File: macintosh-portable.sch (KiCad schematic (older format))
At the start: 0 parts

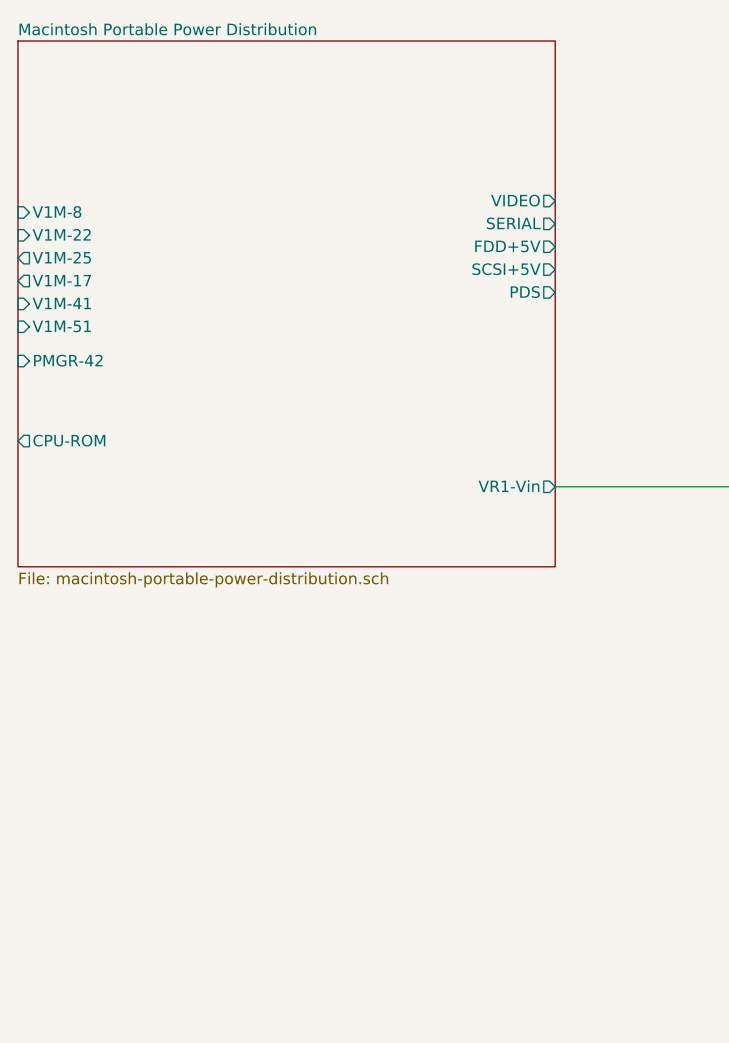
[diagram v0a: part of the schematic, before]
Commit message: Added V1M module.
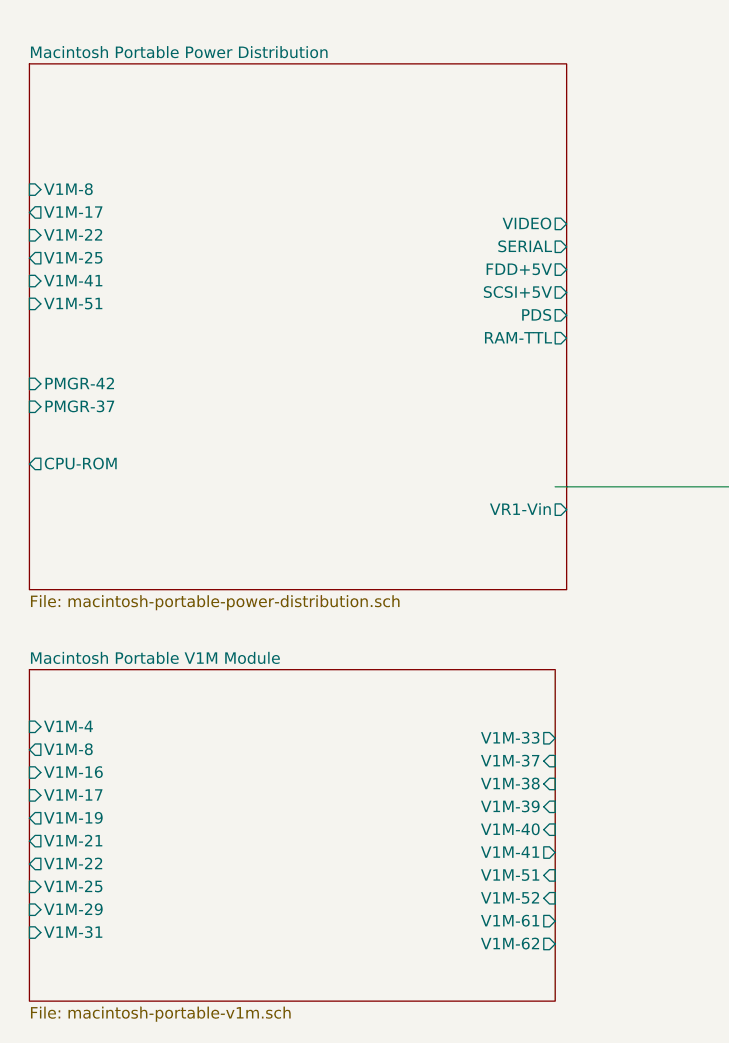
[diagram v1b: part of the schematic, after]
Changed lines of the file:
@@
 $Descr A4 11693 8268
 encoding utf-8
-Sheet 1 3
+Sheet 1 4
 Title ""
 Date ""
@@
 $EndDescr
 $Sheet
-S 1150 1400 2350 2300
+S 1200 1500 2350 2300
 U 5CE45908
 F0 "Macintosh Portable Power Distribution" 50
 F1 "macintosh-portable-power-distribution.sch" 50
-F2 "VR1-Vin" O R 3500 3350 50
-F3 "V1M-41" I L 1150 2550 50
-F4 "V1M-51" I L 1150 2650 50
-F5 "PMGR-42" I L 1150 2800 50
-F6 "SCSI+5V" O R 3500 2400 50
-F7 "V1M-8" I L 1150 2150 50
-F8 "FDD+5V" O R 3500 2300 50
-F9 "CPU-ROM" O L 1150 3150 50
-F10 "PDS" O R 3500 2500 50
-F11 "VIDEO" O R 3500 2100 50
-F12 "SERIAL" O R 3500 2200 50
-F13 "V1M-25" O L 1150 2350 50
-F14 "V1M-17" O L 1150 2450 50
-F15 "V1M-22" I L 1150 2250 50
+F2 "VR1-Vin" O R 3550 3450 50
+F3 "V1M-41" I L 1200 2450 50
+F4 "V1M-51" I L 1200 2550 50
+F5 "PMGR-42" I L 1200 2900 50
+F6 "SCSI+5V" O R 3550 2500 50
+F7 "V1M-8" I L 1200 2050 50
+F8 "FDD+5V" O R 3550 2400 50
+F9 "CPU-ROM" O L 1200 3250 50
+F10 "PDS" O R 3550 2600 50
+F11 "VIDEO" O R 3550 2200 50
+F12 "SERIAL" O R 3550 2300 50
+F13 "V1M-25" O L 1200 2350 50
+F14 "V1M-17" O L 1200 2150 50
+F15 "V1M-22" I L 1200 2250 50
+F16 "RAM-TTL" O R 3550 2700 50
+F17 "PMGR-37" I L 1200 3000 50
 $EndSheet
 $Sheet
@@
 Wire Wire Line
 	3500 3350 4550 3350
+$Sheet
+S 1200 4150 2300 1450
+U 5CE523FB
+F0 "Macintosh Portable V1M Module" 50
+F1 "macintosh-portable-v1m.sch" 50
+F2 "V1M-22" O L 1200 5000 50
+F3 "V1M-16" I L 1200 4600 50
+F4 "V1M-17" I L 1200 4700 50
+F5 "V1M-40" I R 3500 4850 50
+F6 "V1M-29" I L 1200 5200 50
+F7 "V1M-31" I L 1200 5300 50
+F8 "V1M-25" I L 1200 5100 50
+F9 "V1M-37" I R 3500 4550 50
+F10 "V1M-51" I R 3500 5050 50
+F11 "V1M-52" I R 3500 5150 50
+F12 "V1M-62" O R 3500 5350 50
+F13 "V1M-8" O L 1200 4500 50
+F14 "V1M-4" I L 1200 4400 50
+F15 "V1M-39" I R 3500 4750 50
+F16 "V1M-38" I R 3500 4650 50
+F17 "V1M-41" O R 3500 4950 50
+F18 "V1M-19" O L 1200 4800 50
+F19 "V1M-21" O L 1200 4900 50
+F20 "V1M-33" O R 3500 4450 50
+F21 "V1M-61" O R 3500 5250 50
+$EndSheet
 $EndSCHEMATC

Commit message: Finished V1M, more references on other sheets.
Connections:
- wire segments 1 -> 17
- no-connect marks 0 -> 2
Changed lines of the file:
@@
 encoding utf-8
 Sheet 1 4
-Title ""
-Date ""
-Rev "0.1"
-Comp ""
-Comment1 ""
+Title "Macintosh Portable Power"
+Date "2019-05-27"
+Rev "0.12"
+Comp "https://oldcrap.org"
+Comment1 "Author: Pawel Pieczul"
 Comment2 ""
 Comment3 ""
@@
 $EndDescr
 $Sheet
-S 1200 1500 2350 2300
+S 4100 2100 2350 2400
 U 5CE45908
 F0 "Macintosh Portable Power Distribution" 50
 F1 "macintosh-portable-power-distribution.sch" 50
-F2 "VR1-Vin" O R 3550 3450 50
-F3 "V1M-41" I L 1200 2450 50
-F4 "V1M-51" I L 1200 2550 50
-F5 "PMGR-42" I L 1200 2900 50
-F6 "SCSI+5V" O R 3550 2500 50
-F7 "V1M-8" I L 1200 2050 50
-F8 "FDD+5V" O R 3550 2400 50
-F9 "CPU-ROM" O L 1200 3250 50
-F10 "PDS" O R 3550 2600 50
-F11 "VIDEO" O R 3550 2200 50
-F12 "SERIAL" O R 3550 2300 50
-F13 "V1M-25" O L 1200 2350 50
-F14 "V1M-17" O L 1200 2150 50
-F15 "V1M-22" I L 1200 2250 50
-F16 "RAM-TTL" O R 3550 2700 50
-F17 "PMGR-37" I L 1200 3000 50
+F2 "VR1-Vin" O R 6450 4050 50
+F3 "V1M-41" I L 4100 3450 50
+F4 "V1M-51" I L 4100 3550 50
+F5 "PMGR-42" I L 4100 4150 50
+F6 "SCSI+5V" O R 6450 2650 50
+F7 "V1M-8" I L 4100 2450 50
+F8 "FDD+5V" O R 6450 2550 50
+F9 "CPU-ROM" O R 6450 2950 50
+F10 "PDS" O R 6450 2750 50
+F11 "VIDEO" O R 6450 2450 50
+F12 "V1M-25" O L 4100 3050 50
+F13 "V1M-17" O L 4100 2750 50
+F14 "V1M-22" I L 4100 2950 50
+F15 "RAM-TTL" O R 6450 2850 50
+F16 "PMGR-37" I L 4100 4250 50
+F17 "SERIAL-VCC" O R 6450 3050 50
+F18 "V1M-52" I L 4100 3650 50
+F19 "V1M-39" O L 4100 3350 50
+F20 "V1M-16" O L 4100 2650 50
+F21 "V1M-62" I L 4100 3750 50
+F22 "J21-31" O L 4100 3150 50
+F23 "PMGR-52" O L 4100 4350 50
+F24 "V1M-33" I L 4100 3250 50
+F25 "J9-10" O R 6450 3550 50
+F26 "V1M-18" O L 4100 2850 50
+F27 "V1M-11" O L 4100 2550 50
+F28 "SERIAL-VEE" O R 6450 3150 50
 $EndSheet
 $Sheet
-S 4550 2600 1950 900
+S 6800 3750 1850 450
 U 5CFAA7F4
 F0 "Macintosh Portable 12V Generator Circuit" 50
 F1 "macintosh-portable-12v-generator.sch" 50
-F2 "VR1-Vin" I L 4550 3350 50
-F3 "SCSI+12V" O R 6500 2950 50
-F4 "FDD+12V" O R 6500 3200 50
+F2 "VR1-Vin" I L 6800 4050 50
+F3 "SCSI+12V" O R 8650 3900 50
+F4 "FDD+12V" O R 8650 4050 50
 $EndSheet
 Wire Wire Line
-	3500 3350 4550 3350
+	6450 4050 6800 4050
 $Sheet
-S 1200 4150 2300 1450
+S 1350 900  2350 3600
 U 5CE523FB
 F0 "Macintosh Portable V1M Module" 50
 F1 "macintosh-portable-v1m.sch" 50
-F2 "V1M-22" O L 1200 5000 50
-F3 "V1M-16" I L 1200 4600 50
-F4 "V1M-17" I L 1200 4700 50
-F5 "V1M-40" I R 3500 4850 50
-F6 "V1M-29" I L 1200 5200 50
-F7 "V1M-31" I L 1200 5300 50
-F8 "V1M-25" I L 1200 5100 50
-F9 "V1M-37" I R 3500 4550 50
-F10 "V1M-51" I R 3500 5050 50
-F11 "V1M-52" I R 3500 5150 50
-F12 "V1M-62" O R 3500 5350 50
-F13 "V1M-8" O L 1200 4500 50
-F14 "V1M-4" I L 1200 4400 50
-F15 "V1M-39" I R 3500 4750 50
-F16 "V1M-38" I R 3500 4650 50
-F17 "V1M-41" O R 3500 4950 50
-F18 "V1M-19" O L 1200 4800 50
-F19 "V1M-21" O L 1200 4900 50
-F20 "V1M-33" O R 3500 4450 50
-F21 "V1M-61" O R 3500 5250 50
+F2 "V1M-22" O R 3700 2950 50
+F3 "V1M-16" I R 3700 2650 50
+F4 "V1M-17" I R 3700 2750 50
+F5 "V1M-40" I R 3700 1600 50
+F6 "V1M-29" I L 1350 2200 50
+F7 "V1M-31" I R 3700 3150 50
+F8 "V1M-25" I R 3700 3050 50
+F9 "V1M-37" I R 3700 1300 50
+F10 "V1M-51" O R 3700 3550 50
+F11 "V1M-52" O R 3700 3650 50
+F12 "V1M-62" O R 3700 3750 50
+F13 "V1M-8" O R 3700 2450 50
+F14 "V1M-4" I L 1350 1000 50
+F15 "V1M-39" I R 3700 3350 50
+F16 "V1M-38" I R 3700 1400 50
+F17 "V1M-41" O R 3700 3450 50
+F18 "V1M-19" O L 1350 1700 50
+F19 "V1M-21" O L 1350 1900 50
+F20 "V1M-33" O R 3700 3250 50
+F21 "V1M-61" O R 3700 2100 50
+F22 "V1M-5" O L 1350 1100 50
+F23 "V1M-20" O L 1350 1800 50
+F24 "V1M-36" O R 3700 1200 50
+F25 "V1M-59" O R 3700 2000 50
+F26 "V1M-11" I R 3700 2550 50
+F27 "V1M-18" I R 3700 2850 50
 $EndSheet
+NoConn ~ 1100 1900
+NoConn ~ 3800 2100
+Wire Wire Line
+	3800 2100 3700 2100
+Wire Wire Line
+	1100 1900 1350 1900
+Wire Wire Line
+	3700 2450 4100 2450
+Wire Wire Line
+	3700 2550 4100 2550
+Wire Wire Line
+	4100 2650 3700 2650
+Wire Wire Line
+	4100 2750 3700 2750
+Wire Wire Line
+	4100 2850 3700 2850
+Wire Wire Line
+	3700 2950 4100 2950
+Wire Wire Line
+	4100 3050 3700 3050
+Wire Wire Line
+	4100 3150 3700 3150
+Wire Wire Line
+	3700 3250 4100 3250
+Wire Wire Line
+	4100 3350 3700 3350
+Wire Wire Line
+	3700 3450 4100 3450
+Wire Wire Line
+	3700 3550 4100 3550
+Wire Wire Line
+	3700 3650 4100 3650
+Wire Wire Line
+	3700 3750 4100 3750
 $EndSCHEMATC

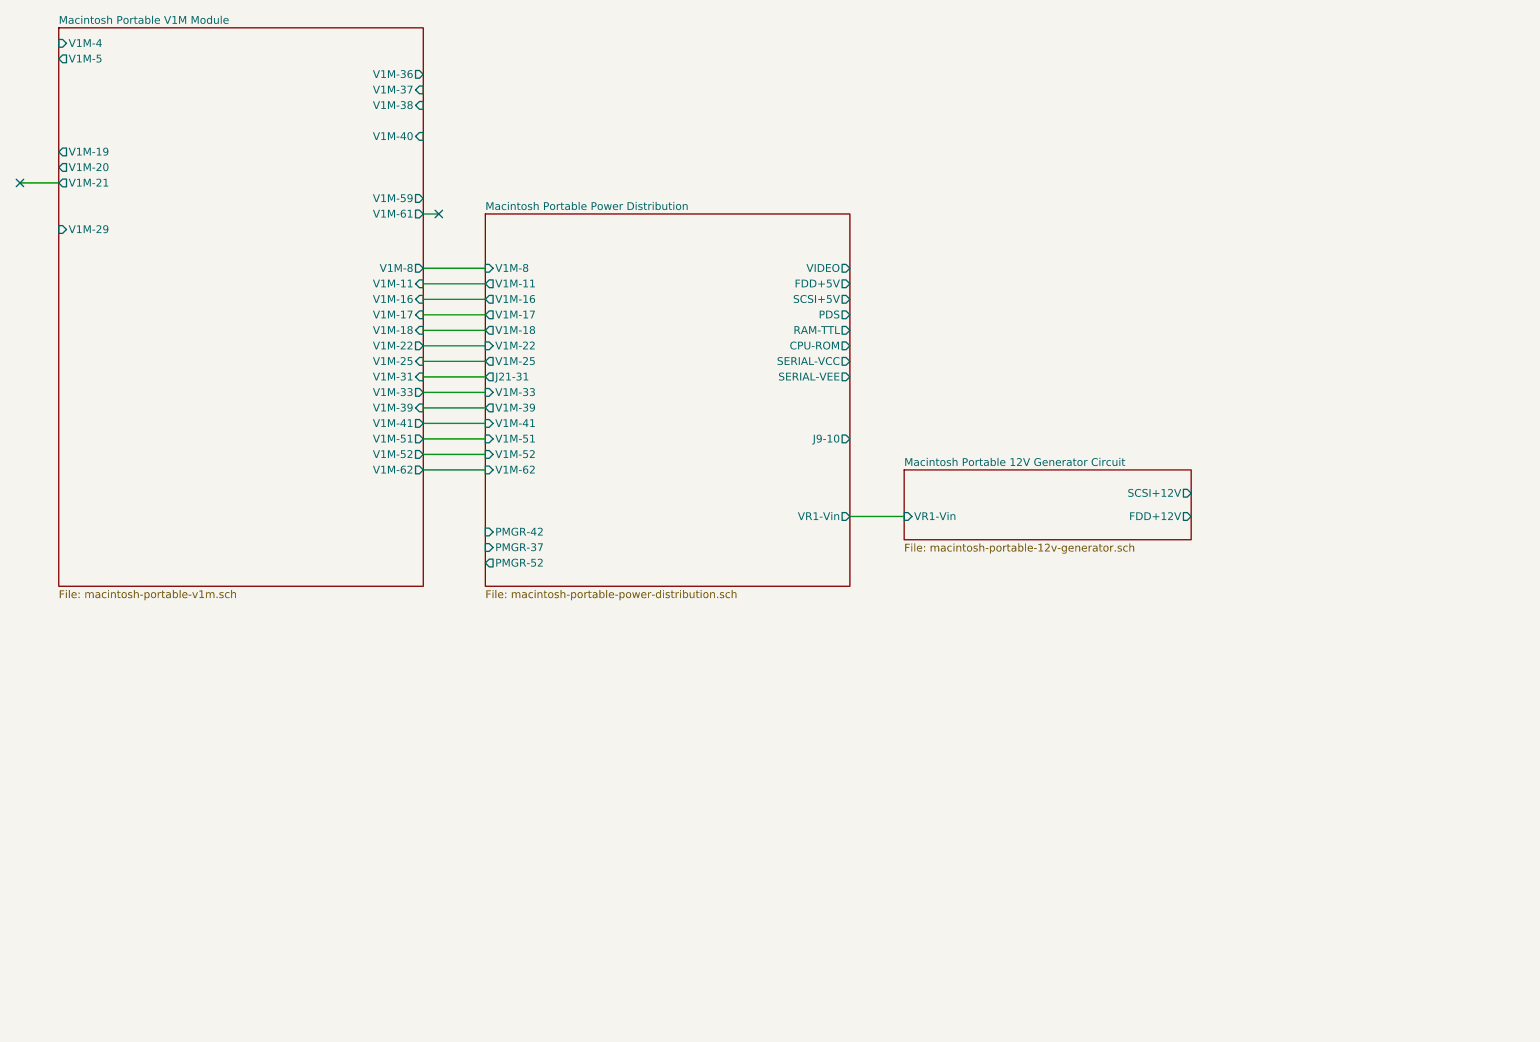
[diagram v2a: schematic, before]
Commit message: Symbol library cleanup
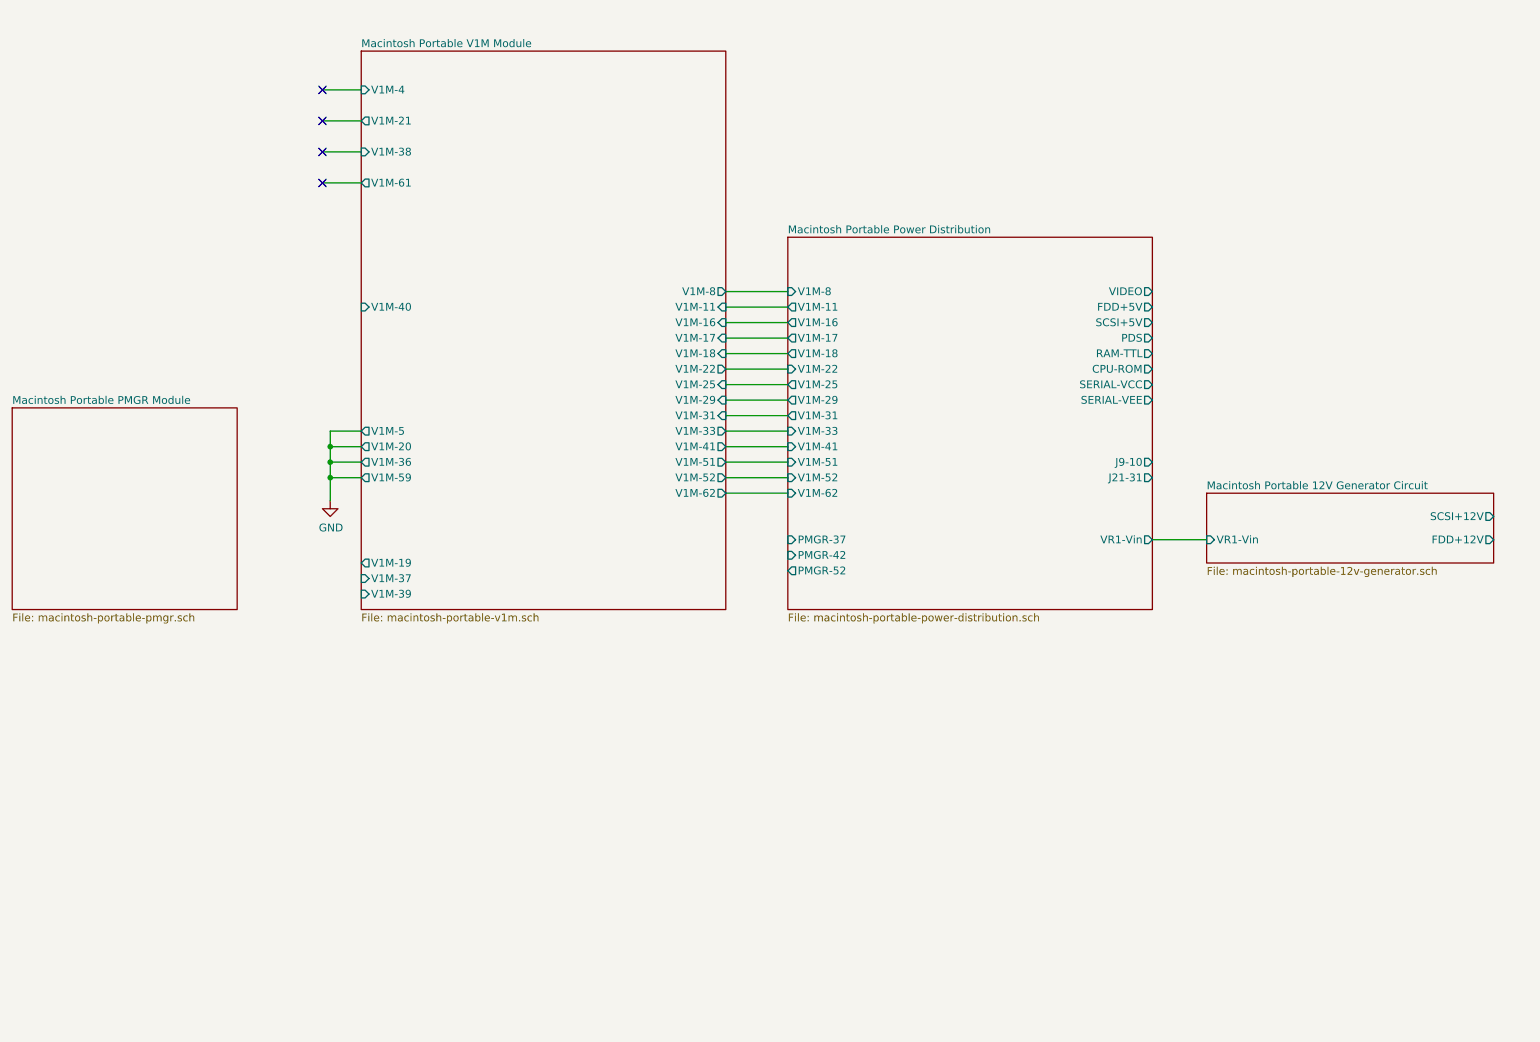
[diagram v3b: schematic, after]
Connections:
- no-connect marks 2 -> 4
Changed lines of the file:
@@
 $Descr A4 11693 8268
 encoding utf-8
-Sheet 1 4
+Sheet 1 5
 Title "Macintosh Portable Power"
 Date "2019-05-27"
@@
 $EndDescr
 $Sheet
-S 4100 2100 2350 2400
+S 6050 2250 2350 2400
 U 5CE45908
 F0 "Macintosh Portable Power Distribution" 50
 F1 "macintosh-portable-power-distribution.sch" 50
-F2 "VR1-Vin" O R 6450 4050 50
-F3 "V1M-41" I L 4100 3450 50
-F4 "V1M-51" I L 4100 3550 50
-F5 "PMGR-42" I L 4100 4150 50
-F6 "SCSI+5V" O R 6450 2650 50
-F7 "V1M-8" I L 4100 2450 50
-F8 "FDD+5V" O R 6450 2550 50
-F9 "CPU-ROM" O R 6450 2950 50
-F10 "PDS" O R 6450 2750 50
-F11 "VIDEO" O R 6450 2450 50
-F12 "V1M-25" O L 4100 3050 50
-F13 "V1M-17" O L 4100 2750 50
-F14 "V1M-22" I L 4100 2950 50
-F15 "RAM-TTL" O R 6450 2850 50
-F16 "PMGR-37" I L 4100 4250 50
-F17 "SERIAL-VCC" O R 6450 3050 50
-F18 "V1M-52" I L 4100 3650 50
-F19 "V1M-39" O L 4100 3350 50
-F20 "V1M-16" O L 4100 2650 50
-F21 "V1M-62" I L 4100 3750 50
-F22 "J21-31" O L 4100 3150 50
-F23 "PMGR-52" O L 4100 4350 50
-F24 "V1M-33" I L 4100 3250 50
-F25 "J9-10" O R 6450 3550 50
-F26 "V1M-18" O L 4100 2850 50
-F27 "V1M-11" O L 4100 2550 50
-F28 "SERIAL-VEE" O R 6450 3150 50
+F2 "VR1-Vin" O R 8400 4200 50
+F3 "V1M-41" I L 6050 3600 50
+F4 "V1M-51" I L 6050 3700 50
+F5 "PMGR-42" I L 6050 4300 50
+F6 "SCSI+5V" O R 8400 2800 50
+F7 "V1M-8" I L 6050 2600 50
+F8 "FDD+5V" O R 8400 2700 50
+F9 "CPU-ROM" O R 8400 3100 50
+F10 "PDS" O R 8400 2900 50
+F11 "VIDEO" O R 8400 2600 50
+F12 "V1M-25" O L 6050 3200 50
+F13 "V1M-17" O L 6050 2900 50
+F14 "V1M-22" I L 6050 3100 50
+F15 "RAM-TTL" O R 8400 3000 50
+F16 "PMGR-37" I L 6050 4200 50
+F17 "SERIAL-VCC" O R 8400 3200 50
+F18 "V1M-52" I L 6050 3800 50
+F19 "V1M-16" O L 6050 2800 50
+F20 "V1M-62" I L 6050 3900 50
+F21 "J21-31" O R 8400 3800 50
+F22 "PMGR-52" O L 6050 4400 50
+F23 "V1M-33" I L 6050 3500 50
+F24 "J9-10" O R 8400 3700 50
+F25 "V1M-18" O L 6050 3000 50
+F26 "V1M-11" O L 6050 2700 50
+F27 "SERIAL-VEE" O R 8400 3300 50
+F28 "V1M-31" O L 6050 3400 50
+F29 "V1M-29" O L 6050 3300 50
 $EndSheet
 $Sheet
-S 6800 3750 1850 450
+S 8750 3900 1850 450
 U 5CFAA7F4
 F0 "Macintosh Portable 12V Generator Circuit" 50
 F1 "macintosh-portable-12v-generator.sch" 50
-F2 "VR1-Vin" I L 6800 4050 50
-F3 "SCSI+12V" O R 8650 3900 50
-F4 "FDD+12V" O R 8650 4050 50
+F2 "VR1-Vin" I L 8750 4200 50
+F3 "SCSI+12V" O R 10600 4050 50
+F4 "FDD+12V" O R 10600 4200 50
 $EndSheet
 Wire Wire Line
-	6450 4050 6800 4050
+	8400 4200 8750 4200
 $Sheet
-S 1350 900  2350 3600
+S 3300 1050 2350 3600
 U 5CE523FB
 F0 "Macintosh Portable V1M Module" 50
 F1 "macintosh-portable-v1m.sch" 50
-F2 "V1M-22" O R 3700 2950 50
-F3 "V1M-16" I R 3700 2650 50
-F4 "V1M-17" I R 3700 2750 50
-F5 "V1M-40" I R 3700 1600 50
-F6 "V1M-29" I L 1350 2200 50
-F7 "V1M-31" I R 3700 3150 50
-F8 "V1M-25" I R 3700 3050 50
-F9 "V1M-37" I R 3700 1300 50
-F10 "V1M-51" O R 3700 3550 50
-F11 "V1M-52" O R 3700 3650 50
-F12 "V1M-62" O R 3700 3750 50
-F13 "V1M-8" O R 3700 2450 50
-F14 "V1M-4" I L 1350 1000 50
-F15 "V1M-39" I R 3700 3350 50
-F16 "V1M-38" I R 3700 1400 50
-F17 "V1M-41" O R 3700 3450 50
-F18 "V1M-19" O L 1350 1700 50
-F19 "V1M-21" O L 1350 1900 50
-F20 "V1M-33" O R 3700 3250 50
-F21 "V1M-61" O R 3700 2100 50
-F22 "V1M-5" O L 1350 1100 50
-F23 "V1M-20" O L 1350 1800 50
-F24 "V1M-36" O R 3700 1200 50
-F25 "V1M-59" O R 3700 2000 50
-F26 "V1M-11" I R 3700 2550 50
-F27 "V1M-18" I R 3700 2850 50
+F2 "V1M-22" O R 5650 3100 50
+F3 "V1M-16" I R 5650 2800 50
+F4 "V1M-17" I R 5650 2900 50
+F5 "V1M-40" I L 3300 2700 50
+F6 "V1M-29" I R 5650 3300 50
+F7 "V1M-31" I R 5650 3400 50
+F8 "V1M-25" I R 5650 3200 50
+F9 "V1M-37" I L 3300 4450 50
+F10 "V1M-51" O R 5650 3700 50
+F11 "V1M-52" O R 5650 3800 50
+F12 "V1M-62" O R 5650 3900 50
+F13 "V1M-8" O R 5650 2600 50
+F14 "V1M-4" I L 3300 1300 50
+F15 "V1M-39" I L 3300 4550 50
+F16 "V1M-38" I L 3300 1700 50
+F17 "V1M-41" O R 5650 3600 50
+F18 "V1M-19" O L 3300 4350 50
+F19 "V1M-21" O L 3300 1500 50
+F20 "V1M-33" O R 5650 3500 50
+F21 "V1M-61" O L 3300 1900 50
+F22 "V1M-5" O L 3300 3500 50
+F23 "V1M-20" O L 3300 3600 50
+F24 "V1M-36" O L 3300 3700 50
+F25 "V1M-59" O L 3300 3800 50
+F26 "V1M-11" I R 5650 2700 50
+F27 "V1M-18" I R 5650 3000 50
 $EndSheet
-NoConn ~ 1100 1900
-NoConn ~ 3800 2100
+NoConn ~ 3050 1500
 Wire Wire Line
-	3800 2100 3700 2100
+	3050 1500 3300 1500
 Wire Wire Line
-	1100 1900 1350 1900
+	5650 2600 6050 2600
 Wire Wire Line
-	3700 2450 4100 2450
+	5650 2700 6050 2700
 Wire Wire Line
-	3700 2550 4100 2550
+	6050 2800 5650 2800
 Wire Wire Line
-	4100 2650 3700 2650
+	6050 2900 5650 2900
 Wire Wire Line
-	4100 2750 3700 2750
+	6050 3000 5650 3000
 Wire Wire Line
-	4100 2850 3700 2850
+	5650 3100 6050 3100
 Wire Wire Line
-	3700 2950 4100 2950
+	6050 3200 5650 3200
 Wire Wire Line
-	4100 3050 3700 3050
+	6050 3400 5650 3400
 Wire Wire Line
-	4100 3150 3700 3150
+	5650 3500 6050 3500
 Wire Wire Line
-	3700 3250 4100 3250
+	5650 3600 6050 3600
 Wire Wire Line
-	4100 3350 3700 3350
+	5650 3700 6050 3700
 Wire Wire Line
-	3700 3450 4100 3450
+	5650 3800 6050 3800
 Wire Wire Line
-	3700 3550 4100 3550
+	5650 3900 6050 3900
 Wire Wire Line
-	3700 3650 4100 3650
+	5650 3300 6050 3300
+$Comp
+L power:GND #PWR?
+U 1 1 5D0D7706
+P 3100 3950
+F 0 "#PWR?" H 3100 3700 50  0001 C CNN
+F 1 "GND" H 3105 3777 50  0000 C CNN
+F 2 "" H 3100 3950 50  0001 C CNN
+F 3 "" H 3100 3950 50  0001 C CNN
+	1    3100 3950
+	1    0    0    -1
+$EndComp
 Wire Wire Line
-	3700 3750 4100 3750
+	3100 3950 3100 3800
+Wire Wire Line
+	3100 3500 3300 3500
+Wire Wire Line
+	3300 3600 3100 3600
+Connection ~ 3100 3600
+Wire Wire Line
+	3100 3600 3100 3500
+Wire Wire Line
+	3300 3700 3100 3700
+Connection ~ 3100 3700
+Wire Wire Line
+	3100 3700 3100 3600
+Wire Wire Line
+	3300 3800 3100 3800
+Connection ~ 3100 3800
+Wire Wire Line
+	3100 3800 3100 3700
+NoConn ~ 3050 1300
+Wire Wire Line
+	3050 1300 3300 1300
+NoConn ~ 3050 1700
+Wire Wire Line
+	3050 1700 3300 1700
+NoConn ~ 3050 1900
+Wire Wire Line
+	3050 1900 3300 1900
+$Sheet
+S 1050 3350 1450 1300
+U 5D18C0C9
+F0 "Macintosh Portable PMGR Module" 50
+F1 "macintosh-portable-pmgr.sch" 50
+$EndSheet
 $EndSCHEMATC
